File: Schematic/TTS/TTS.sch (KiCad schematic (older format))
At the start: 22 parts, among them J1 Screw_Terminal_01x04, J2 Conn_01x15_Female, J3 Conn_01x15_Female, SW1 SW_DIP_x04, U1 ISL81487EIPZ, U2 MLX90614, U3 MLX90614

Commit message: Updating schematic with Oshpark/Digikey order
Updates to add various components and capability.

2.2 Basic Sensor Suite
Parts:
- removed D3: D, Diode_THT:D_T-1_P5.08mm_Horizontal, symbol Device:D
- added D3: D_Bridge_+AA-, TTS-UART:KBP306GTB, symbol Device:D_Bridge_+AA-
- added R8: 4.7k, Resistor_THT:R_Axial_DIN0204_L3.6mm_D1.6mm_P5.08mm_Horizontal, symbol Device:R
- D1, D2: footprint TTS-UART:DO204-10 -> Diode_SMD:D_SOD-923
- R4, R5, R6, R7: value 100 -> 4.7k; footprint Resistor_THT:R_Axial_DIN0309_L9.0mm_D3.2mm_P12.70mm_Horizontal -> Resistor_THT:R_Axial_DIN0204_L3.6mm_D1.6mm_P5.08mm_Horizontal
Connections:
- net labels added: GND1
- wire segments 108 -> 123
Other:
- moved on the sheet: A1, C1, C2, C3, D1, D2, D4, J1, J2, J3, R1, R2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

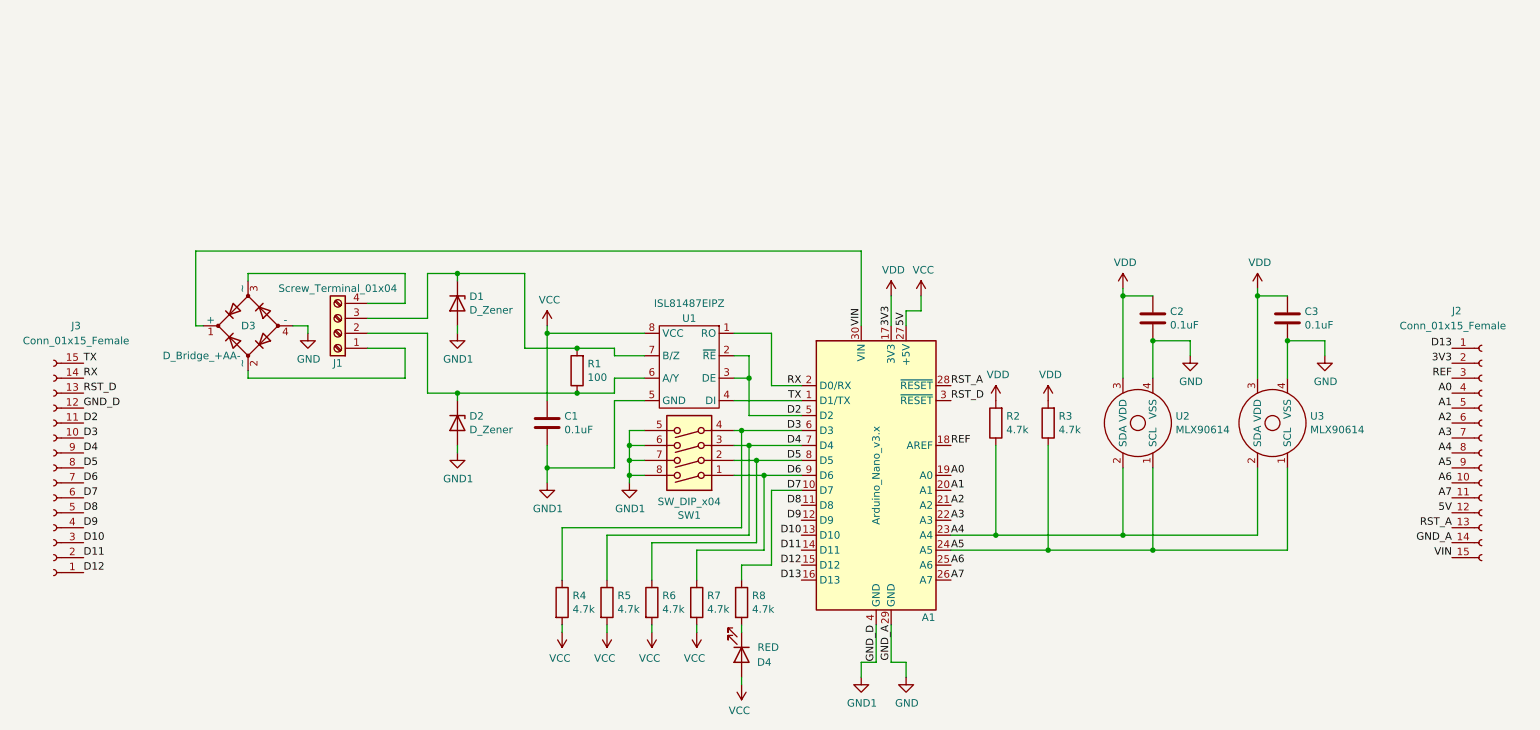
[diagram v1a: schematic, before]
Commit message: Upadeted PCB design for Logger and for TTS
Mega updated for BLE and reduced in size. Nano shield updated for
MLX90621 array based sensor
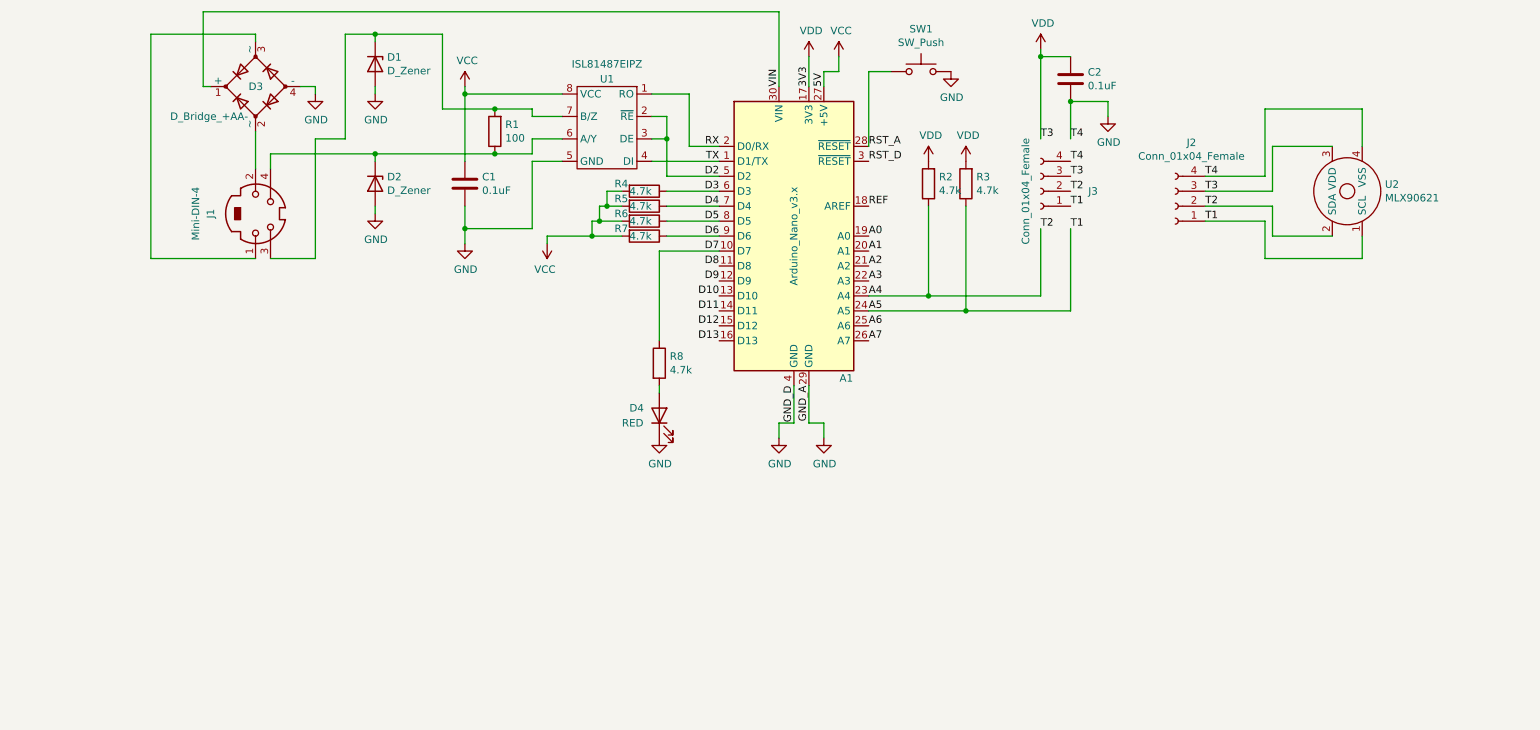
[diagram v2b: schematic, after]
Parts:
- removed C3: 0.1uF, Capacitor_THT:C_Rect_L4.0mm_W2.5mm_P2.50mm, symbol Device:C
- removed J1: Screw_Terminal_01x04, TerminalBlock_Phoenix:TerminalBlock_Phoenix_PT-1,5-4-5.0-H_1x04_P5.00mm_Horizontal, symbol Connector:Screw_Terminal_01x04
- removed J2, J3: Conn_01x15_Female, Connector_PinHeader_2.54mm:PinHeader_1x15_P2.54mm_Vertical, symbol Connector:Conn_01x15_Female
- removed SW1: SW_DIP_x04, Button_Switch_THT:SW_DIP_SPSTx04_Slide_9.78x12.34mm_W7.62mm_P2.54mm, symbol Switch:SW_DIP_x04
- removed U3: MLX90614, TTS-UART:MLX90614ESF-BCC-000-TU, symbol TTS_UART:MLX90614
- added J1: Mini-DIN-4, TTS-URAT:RHT-634-1261-1bottom, symbol Connector:Mini-DIN-4
- added J2, J3: Conn_01x04_Female, Connector_PinSocket_2.54mm:PinSocket_1x04_P2.54mm_Vertical, symbol Connector:Conn_01x04_Female
- added SW1: SW_Push, Connector_PinSocket_2.54mm:PinSocket_1x02_P2.54mm_Vertical, symbol Switch:SW_Push
- D1, D2: footprint Diode_SMD:D_SOD-923 -> Diode_THT:D_DO-41_SOD81_P10.16mm_Horizontal
- D4: footprint digikey-kicad-library:LED_3mm_Radial -> Digikey:LED_3mm_Radial
- U2: value MLX90614 -> MLX90621
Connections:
- net GND1 is gone; now on net GND: A1.4 (GND), C1.2, D1.2 (A), D2.2 (A), U1.5 (GND)
- net A4: now also J2.2 (Pin_2), J3.2 (Pin_2)
- net A5: now also J2.1 (Pin_1), J3.1 (Pin_1)
- net GND: now also D4.1 (K), J2.4 (Pin_4), J3.4 (Pin_4), SW1.2
- net RST_A: now also SW1.1
- net VCC: no longer D4.2 (A)
- net VDD: now also J2.3 (Pin_3), J3.3 (Pin_3)
- net at D2.1 (K), R1.1, U1.6 (A/Y): now also J1.4
- net at D1.1 (K), R1.2, U1.7 (B/Z): now also J1.3
- net at R8.2: now also D4.2 (A); no longer D4.1 (K)
- net at D3.2 (~~): now also J1.2
- net at D3.3 (~~): now also J1.1
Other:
- moved on the sheet: A1, C1, C2, D1, D2, D3, D4, R1, R2, R3, R8, U1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

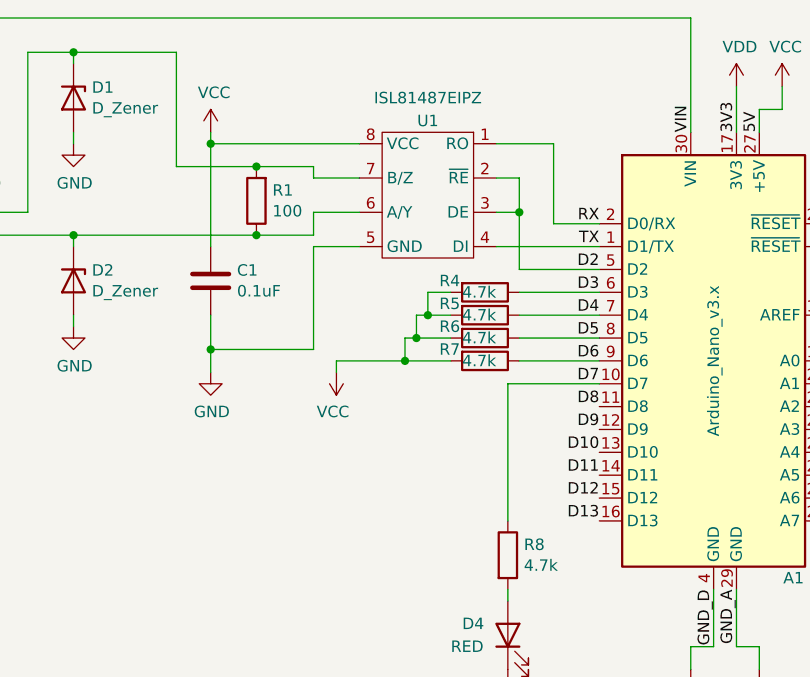
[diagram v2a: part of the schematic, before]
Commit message: Verion 4 PCB and Code
Updated PCB layout for version 4; for both TTS and Logger.
Updated code to asign ID to TTS and to send data via BT
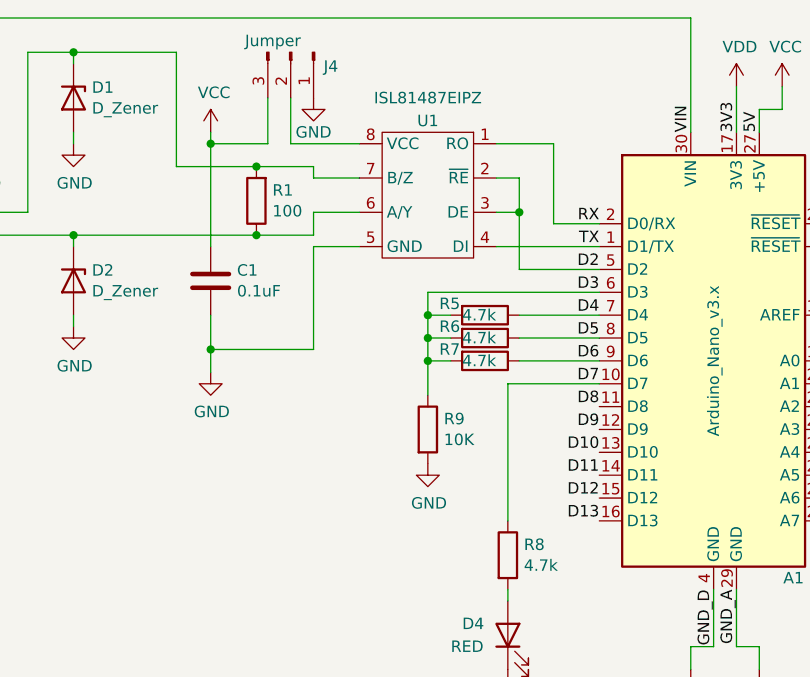
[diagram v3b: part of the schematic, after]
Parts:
- removed R4: 4.7k, Resistor_THT:R_Axial_DIN0204_L3.6mm_D1.6mm_P5.08mm_Horizontal, symbol Device:R
- added J4: Jumper, Connector_PinSocket_2.54mm:PinSocket_1x03_P2.54mm_Vertical, symbol Connector:Conn_01x03_Male
- added R9: 10K, Resistor_THT:R_Axial_DIN0207_L6.3mm_D2.5mm_P7.62mm_Horizontal, symbol Device:R
- J1: footprint TTS-URAT:RHT-634-1261-1bottom -> Connector_PinSocket_2.54mm:PinSocket_2x02_P2.54mm_Vertical
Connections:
- net D3: now also R5.2, R6.2, R7.2, R9.1
- net GND: now also J4.1 (Pin_1), R9.2
- net VCC: now also J4.3 (Pin_3); no longer R5.2, R6.2, R7.2, U1.8 (VCC)
- new net: J4.2 (Pin_2), U1.8 (VCC)
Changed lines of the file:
@@
 Wire Wire Line
 	4350 1600 4150 1600
-Connection ~ 3700 1450
 $Comp
 L power:VCC #PWR0104
@@
 	4150 1750 4150 1850
 Wire Wire Line
-	3700 1900 3700 1450
-Wire Wire Line
 	3700 2200 3700 2350
 Wire Wire Line
@@
 	1    0    0    -1
 $EndComp
-Wire Wire Line
-	4350 1450 3700 1450
 Wire Wire Line
 	5200 1450 4950 1450
@@
 GND_A
 Wire Wire Line
-	3700 1400 3700 1450
-Wire Wire Line
 	5050 2000 5400 2000
 Wire Wire Line
@@
 F 0 "J1" H 2300 1950 50  0000 C CNN
 F 1 "Mini-DIN-4" H 2300 1850 50  0000 C CNN
-F 2 "TTS-URAT:RHT-634-1261-1bottom" H 2300 2250 50  0001 C CNN
+F 2 "Connector_PinSocket_2.54mm:PinSocket_2x02_P2.54mm_Vertical" H 2300 2250 50  0001 C CNN
 F 3 "http://service.powerdynamics.com/ec/Catalog17/Section%2011.pdf" H 2300 2250 50  0001 C CNN
 	1    2300 2250
@@
 Wire Wire Line
 	2400 2550 2700 2550
-$Comp
-L Device:R R4
-U 1 1 6011E9B0
-P 4900 2100
-F 0 "R4" V 4850 1900 50  0000 L CNN
-F 1 "4.7k" V 4900 2000 50  0000 L CNN
-F 2 "Resistor_THT:R_Axial_DIN0204_L3.6mm_D1.6mm_P5.08mm_Horizontal" V 4830 2100 50  0001 C CNN
-F 3 "~" H 4900 2100 50  0001 C CNN
-	1    4900 2100
-	0    1    1    0
-$EndComp
 $Comp
 L Device:R R5
@@
 $EndComp
 Wire Wire Line
-	5400 2100 5050 2100
-Wire Wire Line
 	5400 2200 5050 2200
 Wire Wire Line
@@
 	5400 2400 5050 2400
 Wire Wire Line
-	4750 2400 4550 2400
-Wire Wire Line
-	4250 2400 4250 2450
-Wire Wire Line
-	4750 2300 4600 2300
-Wire Wire Line
-	4550 2300 4550 2400
-Connection ~ 4550 2400
-Wire Wire Line
-	4550 2400 4250 2400
-Wire Wire Line
 	4750 2200 4650 2200
 Wire Wire Line
-	4600 2200 4600 2300
-Connection ~ 4600 2300
-Wire Wire Line
-	4600 2300 4550 2300
-Wire Wire Line
-	4750 2100 4650 2100
-Wire Wire Line
 	4650 2100 4650 2200
-Connection ~ 4650 2200
-Wire Wire Line
-	4650 2200 4600 2200
-$Comp
-L power:VCC #PWR03
-U 1 1 5F97C9F7
-P 4250 2450
-F 0 "#PWR03" H 4250 2300 50  0001 C CNN
-F 1 "VCC" H 4265 2623 50  0000 C CNN
-F 2 "" H 4250 2450 50  0001 C CNN
-F 3 "" H 4250 2450 50  0001 C CNN
-	1    4250 2450
-	-1   0    0    1
-$EndComp
 $Comp
 L power:GND #PWR01
@@
 Text Label 7750 2200 0    50   ~ 0
 T1
+$Comp
+L Device:R R9
+U 1 1 6030A83B
+P 4650 2700
+F 0 "R9" H 4720 2746 50  0000 L CNN
+F 1 "10K" H 4720 2655 50  0000 L CNN
+F 2 "Resistor_THT:R_Axial_DIN0207_L6.3mm_D2.5mm_P7.62mm_Horizontal" V 4580 2700 50  0001 C CNN
+F 3 "~" H 4650 2700 50  0001 C CNN
+	1    4650 2700
+	1    0    0    -1
+$EndComp
+$Comp
+L power:GND #PWR04
+U 1 1 6030B060
+P 4650 2850
+F 0 "#PWR04" H 4650 2600 50  0001 C CNN
+F 1 "GND" H 4655 2677 50  0000 C CNN
+F 2 "" H 4650 2850 50  0001 C CNN
+F 3 "" H 4650 2850 50  0001 C CNN
+	1    4650 2850
+	1    0    0    -1
+$EndComp
+Wire Wire Line
+	4650 2100 5400 2100
+Wire Wire Line
+	4650 2200 4650 2300
+Connection ~ 4650 2200
+Wire Wire Line
+	4750 2300 4650 2300
+Connection ~ 4650 2300
+Wire Wire Line
+	4650 2300 4650 2400
+Wire Wire Line
+	4750 2400 4650 2400
+Connection ~ 4650 2400
+Wire Wire Line
+	4650 2400 4650 2550
+$Comp
+L Connector:Conn_01x03_Male J4
+U 1 1 60333824
+P 4050 1050
+F 0 "J4" V 4112 1194 50  0000 L CNN
+F 1 "Jumper" V 4000 850 50  0000 L CNN
+F 2 "Connector_PinSocket_2.54mm:PinSocket_1x03_P2.54mm_Vertical" H 4050 1050 50  0001 C CNN
+F 3 "~" H 4050 1050 50  0001 C CNN
+	1    4050 1050
+	0    1    1    0
+$EndComp
+Wire Wire Line
+	3700 1400 3700 1450
+Wire Wire Line
+	3950 1250 3950 1450
+Wire Wire Line
+	3950 1450 3700 1450
+Connection ~ 3700 1450
+Wire Wire Line
+	3700 1450 3700 1900
+Wire Wire Line
+	4050 1250 4050 1450
+Wire Wire Line
+	4050 1450 4350 1450
+$Comp
+L power:GND #PWR0113
+U 1 1 6033DB98
+P 4150 1250
+F 0 "#PWR0113" H 4150 1000 50  0001 C CNN
+F 1 "GND" H 4150 1100 50  0000 C CNN
+F 2 "" H 4150 1250 50  0001 C CNN
+F 3 "" H 4150 1250 50  0001 C CNN
+	1    4150 1250
+	1    0    0    -1
+$EndComp
 $EndSCHEMATC
